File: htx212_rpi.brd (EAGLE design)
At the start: 40.9 x 33.5 mm, 31 parts, among them IC1 LM358N, X1 MIC, X12 SPK, X13 GND, X15 DCD, X2 GND, X3 PTT, X4 7.5V, X5 GND, X6 MIC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

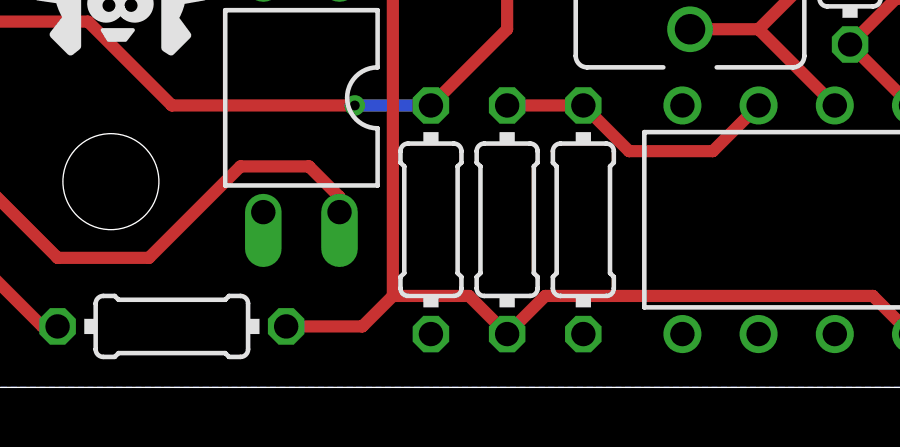
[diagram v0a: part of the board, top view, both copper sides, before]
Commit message: PTT pull-down to pull-up on PTT, radio side.
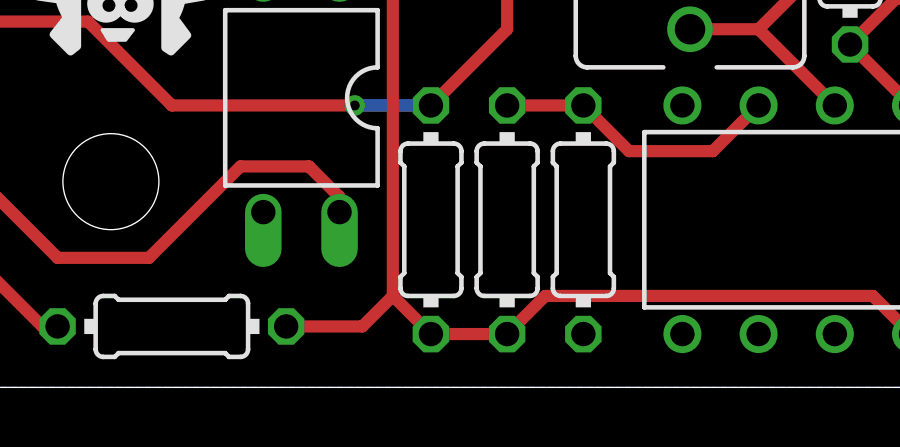
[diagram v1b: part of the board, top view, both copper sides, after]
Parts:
- X4: value 7.5V -> 5V
- X6: value MIC -> SPK
- X7: value SPK -> MIC
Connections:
- net GND: no longer R9.2
- net VCC: now also R9.2
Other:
- board text added: "R0.2"
- board text removed: "R0.1"
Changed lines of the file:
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@@
 <text x="8.128" y="10.16" size="0.8128" layer="27" font="vector" ratio="10" align="bottom-center">cc-by-sa</text>
 <text x="20.828" y="30.226" size="0.8128" layer="27" font="vector" ratio="10" align="bottom-center">www.bot-thoughts.com</text>
-<text x="31.75" y="31.75" size="1.016" layer="27" font="vector" ratio="10">R0.1</text>
+<text x="31.75" y="31.75" size="1.016" layer="27" font="vector" ratio="10">R0.2</text>
 </plain>
 <attributes>
@@
 <element name="X1" library="bt_electromech" package="PAD_22GA" value="MIC" x="38.608" y="12.954" rot="R180"/>
 <element name="X3" library="bt_electromech" package="PAD_22GA" value="PTT" x="38.608" y="18.034" rot="R180"/>
-<element name="X4" library="bt_electromech" package="PAD_22GA" value="7.5V" x="38.608" y="20.574" rot="R180"/>
+<element name="X4" library="bt_electromech" package="PAD_22GA" value="5V" x="38.608" y="20.574" rot="R180"/>
 <element name="X5" library="bt_electromech" package="PAD_22GA" value="GND" x="38.608" y="15.494" rot="R180"/>
-<element name="X6" library="bt_electromech" package="PAD_22GA" value="MIC" x="1.778" y="20.574"/>
-<element name="X7" library="bt_electromech" package="PAD_22GA" value="SPK" x="1.778" y="29.21"/>
+<element name="X6" library="bt_electromech" package="PAD_22GA" value="SPK" x="1.778" y="20.574"/>
+<element name="X7" library="bt_electromech" package="PAD_22GA" value="MIC" x="1.778" y="29.21"/>
 <element name="X12" library="bt_electromech" package="PAD_22GA" value="SPK" x="38.608" y="25.654" rot="R180"/>
 <element name="X13" library="bt_electromech" package="PAD_22GA" value="GND" x="38.608" y="23.114" rot="R180"/>
@@
 <contactref element="OK3" pad="3"/>
 <contactref element="R6" pad="2"/>
-<contactref element="R9" pad="2"/>
 <contactref element="IC1" pad="4"/>
 <contactref element="X2" pad="P$1"/>
@@
 <wire x1="37.592" y1="1.778" x2="34.544" y2="1.778" width="0.4064" layer="1"/>
 <wire x1="13.716" y1="2.032" x2="16.256" y2="2.032" width="0.4064" layer="1"/>
-<wire x1="16.256" y1="2.032" x2="17.272" y2="3.048" width="0.4064" layer="1"/>
-<wire x1="17.272" y1="3.048" x2="19.812" y2="3.048" width="0.4064" layer="1"/>
-<wire x1="19.812" y1="3.048" x2="21.082" y2="1.778" width="0.4064" layer="1"/>
 <wire x1="21.082" y1="1.778" x2="22.352" y2="3.048" width="0.4064" layer="1"/>
 <wire x1="22.352" y1="3.048" x2="33.274" y2="3.048" width="0.4064" layer="1"/>
@@
 <wire x1="40.132" y1="19.558" x2="40.132" y2="4.318" width="0.4064" layer="1"/>
 <wire x1="40.132" y1="4.318" x2="37.592" y2="1.778" width="0.4064" layer="1"/>
+<contactref element="R9" pad="2"/>
+<wire x1="21.082" y1="1.778" x2="18.542" y2="1.778" width="0.4064" layer="1"/>
+<wire x1="18.542" y1="1.778" x2="17.272" y2="3.048" width="0.4064" layer="1"/>
+<wire x1="16.256" y1="2.032" x2="17.272" y2="3.048" width="0.4064" layer="1"/>
 </signal>
 <signal name="PI_IN">
